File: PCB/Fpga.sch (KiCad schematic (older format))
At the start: 52 parts, among them U12 10CL010, U13 ECS-5032MV

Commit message: Add additional mounting holes, optimize receive power supply connections for layout, simplify FPGA analog ground, layout 3v3 and 1v2 supplies
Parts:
- removed NT5: Net-Tie_2, Parts:NetTie-2, symbol Device:Net-Tie_2
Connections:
- net GNDA-FPGA is gone; now on net GND: C47.2, C48.2, C49.2, U12.108 (GNDA2), U12.36 (GNDA1)
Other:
- note added: "Layout GNDA traces to minimize noise."
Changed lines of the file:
@@
 $EndComp
 $Comp
-L power:GND #PWR0111
+L power:GND #PWR0110
 U 1 1 5DE22333
 P 1200 4250
-F 0 "#PWR0111" H 1200 4000 50  0001 C CNN
+F 0 "#PWR0110" H 1200 4000 50  0001 C CNN
 F 1 "GND" H 1205 4077 50  0000 C CNN
 F 2 "" H 1200 4250 50  0001 C CNN
@@
 Wire Wire Line
 	1200 3700 1350 3700
-$Comp
-L Parts:GNDA-FPGA #PWR0110
-U 1 1 5DE2E502
-P 800 4250
-F 0 "#PWR0110" H 800 4000 50  0001 C CNN
-F 1 "GNDA-FPGA" H 805 4077 50  0000 C CNN
-F 2 "" H 800 4250 50  0001 C CNN
-F 3 "" H 800 4250 50  0001 C CNN
-	1    800  4250
-	1    0    0    -1
-$EndComp
-Wire Wire Line
-	1200 3700 1200 4200
-$Comp
-L Device:Net-Tie_2 NT5
-U 1 1 5DE2A792
-P 1000 4200
-F 0 "NT5" H 1000 4381 50  0000 C CNN
-F 1 "Net-Tie_2" H 1000 4290 50  0000 C CNN
-F 2 "Parts:NetTie-2" H 1000 4200 50  0001 C CNN
-F 3 "~" H 1000 4200 50  0001 C CNN
-	1    1000 4200
-	1    0    0    -1
-$EndComp
-Wire Wire Line
-	1100 4200 1200 4200
-Wire Wire Line
-	800  4200 800  4250
-Connection ~ 800  4200
-Wire Wire Line
-	900  4200 800  4200
-Wire Wire Line
-	800  3900 800  4200
+Wire Wire Line
+	1200 3700 1200 4000
 Wire Wire Line
 	1300 3900 1300 4000
-Wire Wire Line
-	800  3900 1300 3900
-Connection ~ 1300 3900
 Wire Wire Line
 	1300 3900 1350 3900
@@
 	1650 5850 1700 5850
 $Comp
-L power:GND #PWR0121
+L power:GND #PWR0120
 U 1 1 5DD8EAB5
 P 1650 5850
-F 0 "#PWR0121" H 1650 5600 50  0001 C CNN
+F 0 "#PWR0120" H 1650 5600 50  0001 C CNN
 F 1 "GND" V 1650 5675 50  0000 C CNN
 F 2 "" H 1650 5850 50  0001 C CNN
@@
 $EndComp
 $Comp
-L power:+2V5 #PWR0119
+L power:+2V5 #PWR0118
 U 1 1 5DD94A03
 P 1400 5750
-F 0 "#PWR0119" H 1400 5600 50  0001 C CNN
+F 0 "#PWR0118" H 1400 5600 50  0001 C CNN
 F 1 "+2V5" V 1400 5950 50  0000 C CNN
 F 2 "" H 1400 5750 50  0001 C CNN
@@
 $EndComp
 $Comp
-L power:+3V3 #PWR0114
+L power:+3V3 #PWR0113
 U 1 1 5DEE2282
 P 1700 5350
-F 0 "#PWR0114" H 1700 5200 50  0001 C CNN
+F 0 "#PWR0113" H 1700 5200 50  0001 C CNN
 F 1 "+3V3" V 1700 5450 50  0000 L CNN
 F 2 "" H 1700 5350 50  0001 C CNN
@@
 $EndComp
 $Comp
-L power:+3V3 #PWR0118
+L power:+3V3 #PWR0117
 U 1 1 5DDACD3F
 P 1150 5650
-F 0 "#PWR0118" H 1150 5500 50  0001 C CNN
+F 0 "#PWR0117" H 1150 5500 50  0001 C CNN
 F 1 "+3V3" V 1150 5750 50  0000 L CNN
 F 2 "" H 1150 5650 50  0001 C CNN
@@
 $EndComp
 $Comp
-L power:+2V5 #PWR0122
+L power:+2V5 #PWR0121
 U 1 1 5DDADC93
 P 1900 5950
-F 0 "#PWR0122" H 1900 5800 50  0001 C CNN
+F 0 "#PWR0121" H 1900 5800 50  0001 C CNN
 F 1 "+2V5" V 1900 6150 50  0000 C CNN
 F 2 "" H 1900 5950 50  0001 C CNN
@@
 $EndComp
 $Comp
-L power:+2V5 #PWR0123
+L power:+2V5 #PWR0122
 U 1 1 5DDADF3E
 P 2150 6050
-F 0 "#PWR0123" H 2150 5900 50  0001 C CNN
+F 0 "#PWR0122" H 2150 5900 50  0001 C CNN
 F 1 "+2V5" V 2150 6250 50  0000 C CNN
 F 2 "" H 2150 6050 50  0001 C CNN
@@
 $EndComp
 $Comp
-L power:+3V3 #PWR0126
+L power:+3V3 #PWR0125
 U 1 1 5DDB0FE1
 P 1850 6450
-F 0 "#PWR0126" H 1850 6300 50  0001 C CNN
+F 0 "#PWR0125" H 1850 6300 50  0001 C CNN
 F 1 "+3V3" V 1850 6550 50  0000 L CNN
 F 2 "" H 1850 6450 50  0001 C CNN
@@
 $EndComp
 $Comp
-L power:+3V3 #PWR0128
+L power:+3V3 #PWR0127
 U 1 1 5DDB15B2
 P 1600 6850
-F 0 "#PWR0128" H 1600 6700 50  0001 C CNN
+F 0 "#PWR0127" H 1600 6700 50  0001 C CNN
 F 1 "+3V3" V 1600 6950 50  0000 L CNN
 F 2 "" H 1600 6850 50  0001 C CNN
@@
 $EndComp
 $Comp
-L power:+3V3 #PWR0129
+L power:+3V3 #PWR0128
 U 1 1 5DDB1889
 P 1850 6950
-F 0 "#PWR0129" H 1850 6800 50  0001 C CNN
+F 0 "#PWR0128" H 1850 6800 50  0001 C CNN
 F 1 "+3V3" V 1850 7050 50  0000 L CNN
 F 2 "" H 1850 6950 50  0001 C CNN
@@
 $EndComp
 $Comp
-L power:GND #PWR0124
+L power:GND #PWR0123
 U 1 1 5DDB19BB
 P 2600 6150
-F 0 "#PWR0124" H 2600 5900 50  0001 C CNN
+F 0 "#PWR0123" H 2600 5900 50  0001 C CNN
 F 1 "GND" V 2600 5975 50  0000 C CNN
 F 2 "" H 2600 6150 50  0001 C CNN
@@
 $EndComp
 $Comp
-L power:GND #PWR0127
+L power:GND #PWR0126
 U 1 1 5DDB20C5
 P 2550 6650
-F 0 "#PWR0127" H 2550 6400 50  0001 C CNN
+F 0 "#PWR0126" H 2550 6400 50  0001 C CNN
 F 1 "GND" V 2550 6475 50  0000 C CNN
 F 2 "" H 2550 6650 50  0001 C CNN
@@
 $EndComp
 $Comp
-L power:+3V3 #PWR0117
+L power:+3V3 #PWR0116
 U 1 1 5DF0EC9E
 P 900 5550
-F 0 "#PWR0117" H 900 5400 50  0001 C CNN
+F 0 "#PWR0116" H 900 5400 50  0001 C CNN
 F 1 "+3V3" V 900 5650 50  0000 L CNN
 F 2 "" H 900 5550 50  0001 C CNN
@@
 $EndComp
 $Comp
-L power:+3V3 #PWR0115
+L power:+3V3 #PWR0114
 U 1 1 5DF40C3D
 P 1950 5450
-F 0 "#PWR0115" H 1950 5300 50  0001 C CNN
+F 0 "#PWR0114" H 1950 5300 50  0001 C CNN
 F 1 "+3V3" V 1950 5550 50  0000 L CNN
 F 2 "" H 1950 5450 50  0001 C CNN
@@
 $EndComp
 $Comp
-L power:+1V2 #PWR0113
+L power:+1V2 #PWR0112
 U 1 1 5DEA2FAA
 P 8450 5050
-F 0 "#PWR0113" H 8450 4900 50  0001 C CNN
+F 0 "#PWR0112" H 8450 4900 50  0001 C CNN
 F 1 "+1V2" H 8465 5223 50  0000 C CNN
 F 2 "" H 8450 5050 50  0001 C CNN
@@
 Connection ~ 8850 5400
 $Comp
-L power:GND #PWR0116
+L power:GND #PWR0115
 U 1 1 5DEB9767
 P 8450 5450
-F 0 "#PWR0116" H 8450 5200 50  0001 C CNN
+F 0 "#PWR0115" H 8450 5200 50  0001 C CNN
 F 1 "GND" H 8455 5277 50  0000 C CNN
 F 2 "" H 8450 5450 50  0001 C CNN
@@
 Connection ~ 10500 5400
 $Comp
-L power:+3V3 #PWR0120
+L power:+3V3 #PWR0119
 U 1 1 5DEEB0E4
 P 7100 5800
-F 0 "#PWR0120" H 7100 5650 50  0001 C CNN
+F 0 "#PWR0119" H 7100 5650 50  0001 C CNN
 F 1 "+3V3" H 7115 5973 50  0000 C CNN
 F 2 "" H 7100 5800 50  0001 C CNN
@@
 Connection ~ 8500 6150
 $Comp
-L power:GND #PWR0125
+L power:GND #PWR0124
 U 1 1 5DF36B33
 P 7100 6200
-F 0 "#PWR0125" H 7100 5950 50  0001 C CNN
+F 0 "#PWR0124" H 7100 5950 50  0001 C CNN
 F 1 "GND" H 7105 6027 50  0000 C CNN
 F 2 "" H 7100 6200 50  0001 C CNN
@@
 Connection ~ 8800 4550
 $Comp
-L power:GND #PWR0112
+L power:GND #PWR0111
 U 1 1 5E068FA4
 P 8450 4600
-F 0 "#PWR0112" H 8450 4350 50  0001 C CNN
+F 0 "#PWR0111" H 8450 4350 50  0001 C CNN
 F 1 "GND" H 8455 4427 50  0000 C CNN
 F 2 "" H 8450 4600 50  0001 C CNN
@@
 VGA-D1
 $Comp
-L Parts:GNDA-FPGA #PWR0106
-U 1 1 5DFAA090
-P 10050 2900
-F 0 "#PWR0106" H 10050 2650 50  0001 C CNN
-F 1 "GNDA-FPGA" H 10055 2727 50  0000 C CNN
-F 2 "" H 10050 2900 50  0001 C CNN
-F 3 "" H 10050 2900 50  0001 C CNN
-	1    10050 2900
-	1    0    0    -1
-$EndComp
-$Comp
 L Device:C_Small C49
 U 1 1 5E10DD5E
@@
 $EndComp
 Wire Wire Line
-	10450 2850 10850 2850
-Wire Wire Line
 	10850 2850 10850 2800
 Connection ~ 10450 2850
@@
 Wire Wire Line
 	4500 1000 4200 1000
+$Comp
+L power:GND #PWR0106
+U 1 1 5E42C3C3
+P 10050 2900
+F 0 "#PWR0106" H 10050 2650 50  0001 C CNN
+F 1 "GND" H 10055 2727 50  0000 C CNN
+F 2 "" H 10050 2900 50  0001 C CNN
+F 3 "" H 10050 2900 50  0001 C CNN
+	1    10050 2900
+	1    0    0    -1
+$EndComp
+Wire Wire Line
+	10450 2850 10850 2850
+Wire Wire Line
+	1300 4000 1200 4000
+Connection ~ 1300 4000
+Connection ~ 1200 4000
+Wire Wire Line
+	1200 4000 1200 4200
+Text Notes 550  4550 0    50   ~ 0
+Layout GNDA traces to minimize noise.
 $EndSCHEMATC

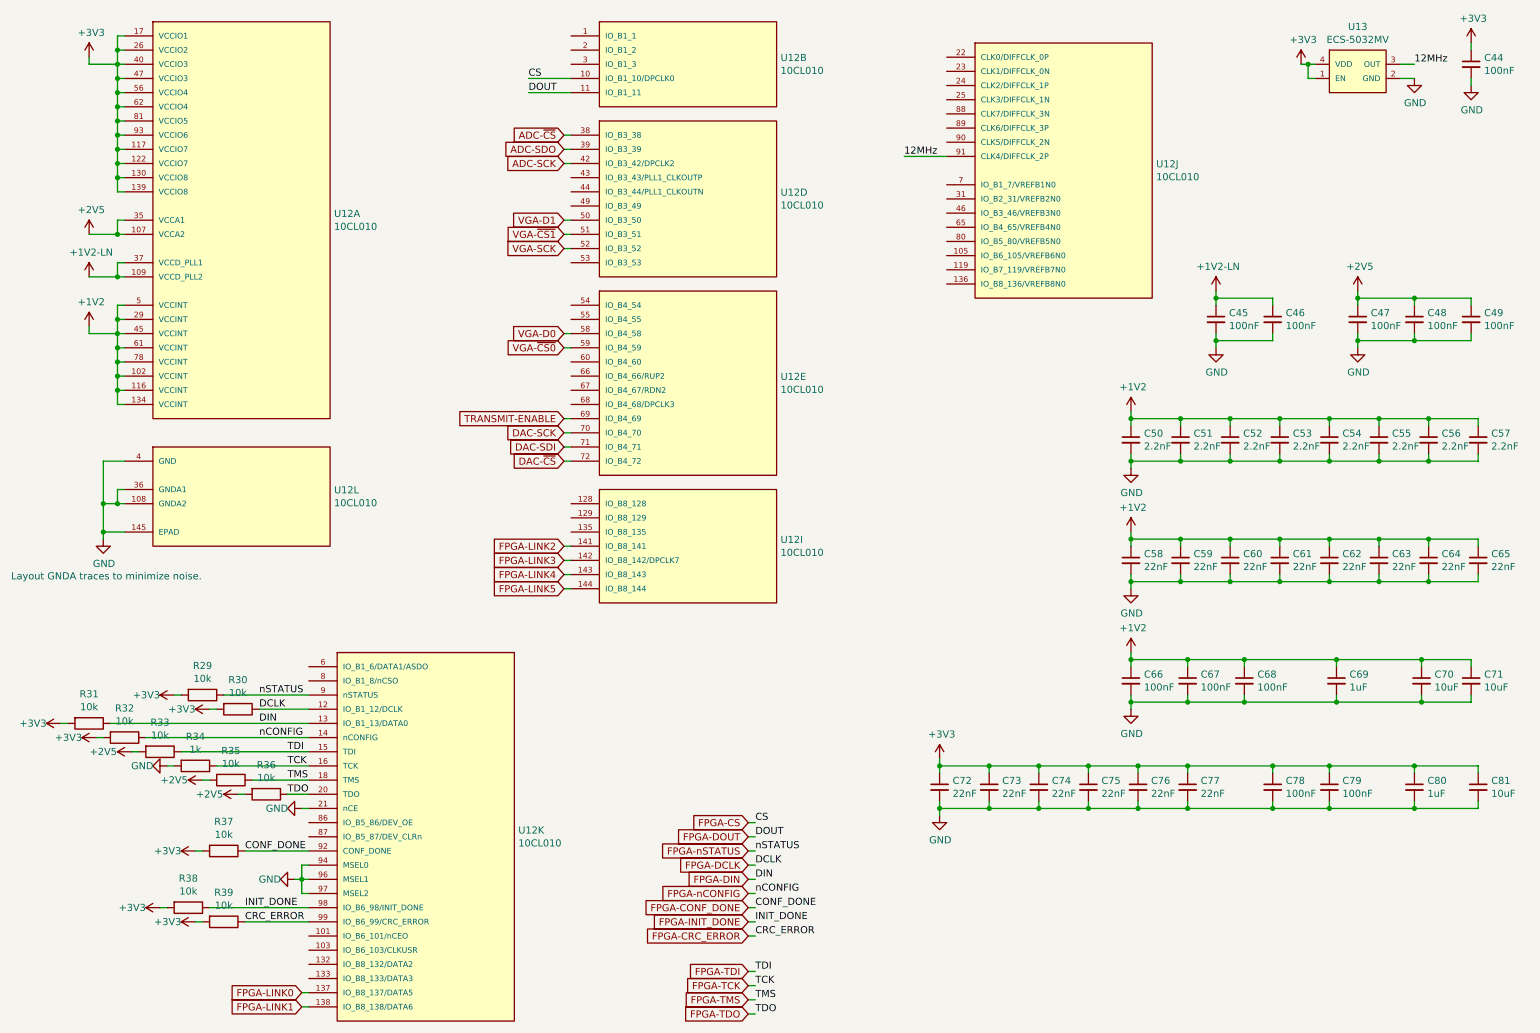
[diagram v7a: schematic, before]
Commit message: Connect more FPGA pins to GND, improve continuity of GND plane
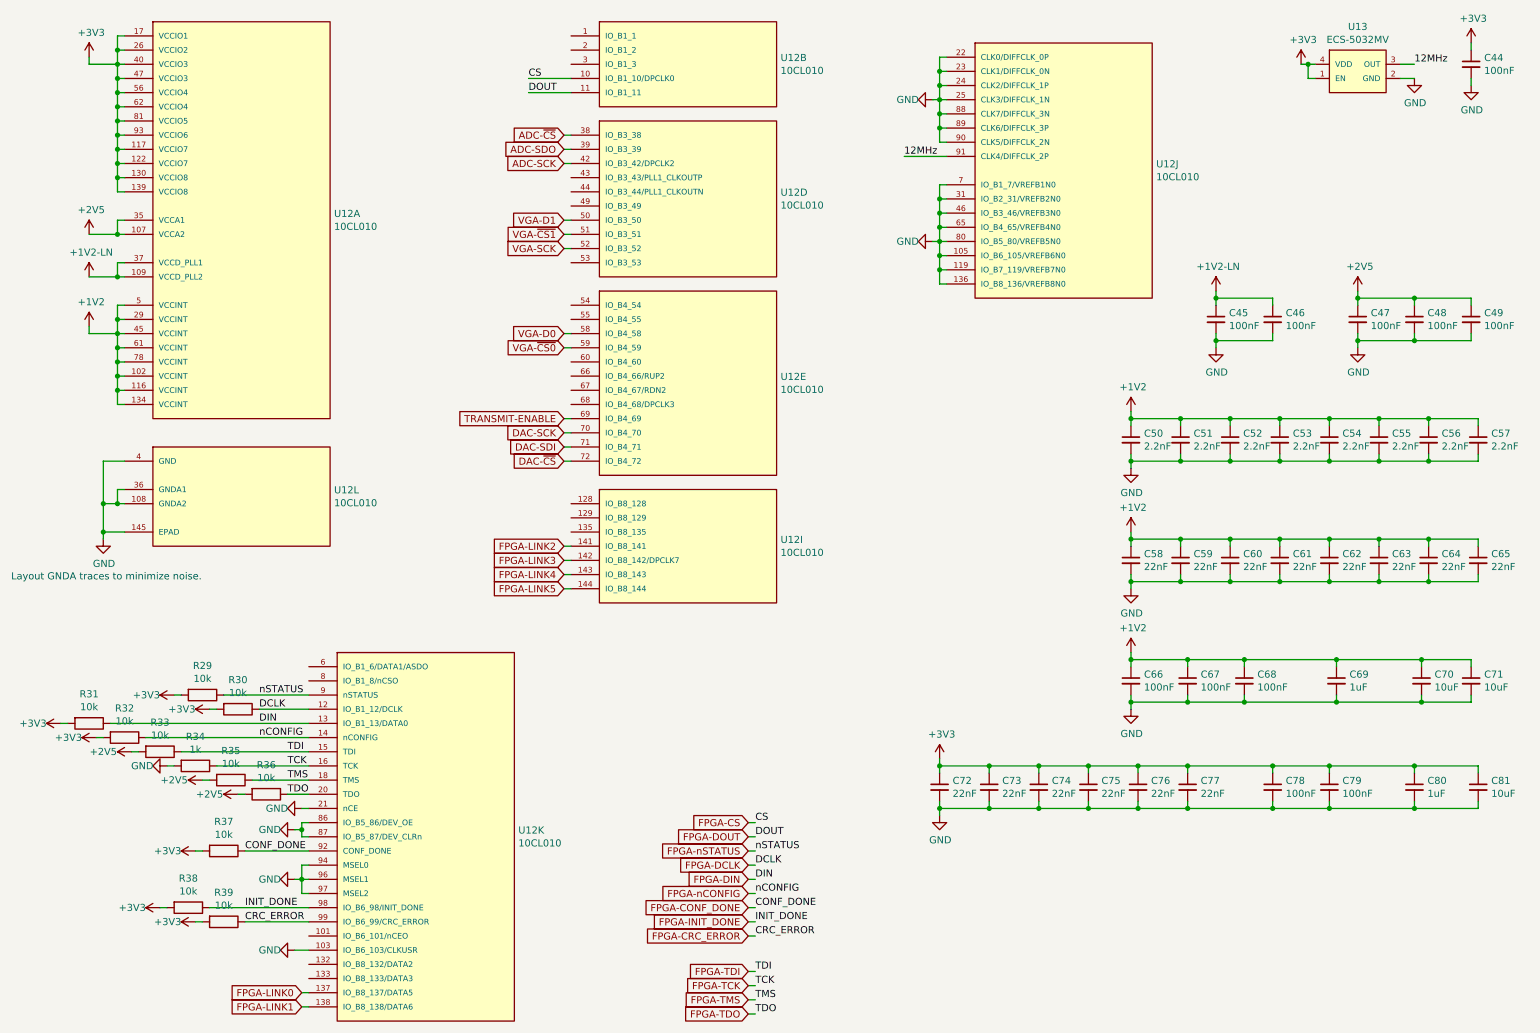
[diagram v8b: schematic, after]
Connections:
- net GND: now also U12.103 (IO_B6_103/CLKUSR), U12.105 (IO_B6_105/VREFB6N0), U12.119 (IO_B7_119/VREFB7N0), U12.136 (IO_B8_136/VREFB8N0), U12.22 (CLK0/DIFFCLK_0P), U12.23 (CLK1/DIFFCLK_0N), U12.24 (CLK2/DIFFCLK_1P), U12.25 (CLK3/DIFFCLK_1N), U12.31 (IO_B2_31/VREFB2N0), U12.46 (IO_B3_46/VREFB3N0), U12.65 (IO_B4_65/VREFB4N0), U12.7 (IO_B1_7/VREFB1N0), U12.80 (IO_B5_80/VREFB5N0), U12.86 (IO_B5_86/DEV_OE), U12.87 (IO_B5_87/DEV_CLRn), U12.88 (CLK7/DIFFCLK_3N), U12.89 (CLK6/DIFFCLK_3P), U12.90 (CLK5/DIFFCLK_2N)
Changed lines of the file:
@@
 Text Notes 550  4550 0    50   ~ 0
 Layout GNDA traces to minimize noise.
+$Comp
+L power:GND #PWR0195
+U 1 1 5E001EDB
+P 7050 1150
+F 0 "#PWR0195" H 7050 900 50  0001 C CNN
+F 1 "GND" V 7050 975 50  0000 C CNN
+F 2 "" H 7050 1150 50  0001 C CNN
+F 3 "" H 7050 1150 50  0001 C CNN
+	1    7050 1150
+	0    1    1    0
+$EndComp
+Wire Wire Line
+	7150 850  7100 850
+Wire Wire Line
+	7100 850  7100 950
+Wire Wire Line
+	7100 1150 7050 1150
+Wire Wire Line
+	7150 950  7100 950
+Connection ~ 7100 950
+Wire Wire Line
+	7100 950  7100 1050
+Wire Wire Line
+	7100 1050 7150 1050
+Connection ~ 7100 1050
+Wire Wire Line
+	7100 1050 7100 1150
+Wire Wire Line
+	7100 1150 7150 1150
+Connection ~ 7100 1150
+Wire Wire Line
+	7100 1150 7100 1250
+Wire Wire Line
+	7100 1250 7150 1250
+Wire Wire Line
+	7100 1250 7100 1350
+Wire Wire Line
+	7100 1350 7150 1350
+Connection ~ 7100 1250
+Wire Wire Line
+	7100 1350 7100 1450
+Wire Wire Line
+	7100 1450 7150 1450
+Connection ~ 7100 1350
+$Comp
+L power:GND #PWR0196
+U 1 1 5E097F21
+P 2550 6300
+F 0 "#PWR0196" H 2550 6050 50  0001 C CNN
+F 1 "GND" V 2550 6125 50  0000 C CNN
+F 2 "" H 2550 6300 50  0001 C CNN
+F 3 "" H 2550 6300 50  0001 C CNN
+	1    2550 6300
+	0    1    1    0
+$EndComp
+Wire Wire Line
+	2550 6300 2600 6300
+Wire Wire Line
+	2600 6300 2600 6250
+Wire Wire Line
+	2600 6250 2650 6250
+Wire Wire Line
+	2600 6300 2600 6350
+Wire Wire Line
+	2600 6350 2650 6350
+Connection ~ 2600 6300
+$Comp
+L power:GND #PWR0197
+U 1 1 5E0C8A61
+P 2550 7150
+F 0 "#PWR0197" H 2550 6900 50  0001 C CNN
+F 1 "GND" V 2550 6975 50  0000 C CNN
+F 2 "" H 2550 7150 50  0001 C CNN
+F 3 "" H 2550 7150 50  0001 C CNN
+	1    2550 7150
+	0    1    1    0
+$EndComp
+Wire Wire Line
+	2550 7150 2650 7150
+$Comp
+L power:GND #PWR?
+U 1 1 5E0F1093
+P 7050 2150
+F 0 "#PWR?" H 7050 1900 50  0001 C CNN
+F 1 "GND" V 7050 1975 50  0000 C CNN
+F 2 "" H 7050 2150 50  0001 C CNN
+F 3 "" H 7050 2150 50  0001 C CNN
+	1    7050 2150
+	0    1    1    0
+$EndComp
+Wire Wire Line
+	7150 1750 7100 1750
+Wire Wire Line
+	7100 1750 7100 1850
+Wire Wire Line
+	7100 2150 7050 2150
+Wire Wire Line
+	7100 2150 7150 2150
+Connection ~ 7100 2150
+Wire Wire Line
+	7150 2050 7100 2050
+Connection ~ 7100 2050
+Wire Wire Line
+	7100 2050 7100 2150
+Wire Wire Line
+	7100 1950 7150 1950
+Connection ~ 7100 1950
+Wire Wire Line
+	7100 1950 7100 2050
+Wire Wire Line
+	7150 1850 7100 1850
+Connection ~ 7100 1850
+Wire Wire Line
+	7100 1850 7100 1950
+Wire Wire Line
+	7100 2150 7100 2250
+Wire Wire Line
+	7100 2250 7150 2250
+Wire Wire Line
+	7100 2250 7100 2350
+Wire Wire Line
+	7100 2350 7150 2350
+Connection ~ 7100 2250
+Wire Wire Line
+	7100 2350 7100 2450
+Wire Wire Line
+	7100 2450 7150 2450
+Connection ~ 7100 2350
 $EndSCHEMATC
